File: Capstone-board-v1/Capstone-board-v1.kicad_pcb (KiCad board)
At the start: 2 copper layers, 22 parts, among them J1 Pico Socket 1, J2 Pico Socket 2, M1 DC Vibration Motor, Q1 2N3904, U1 3.3 V Voltage Regulator, U2 555 Timer, U3 Gyroscope Sensor, U4 OP-Amp, U5 Hall Effect Sensor

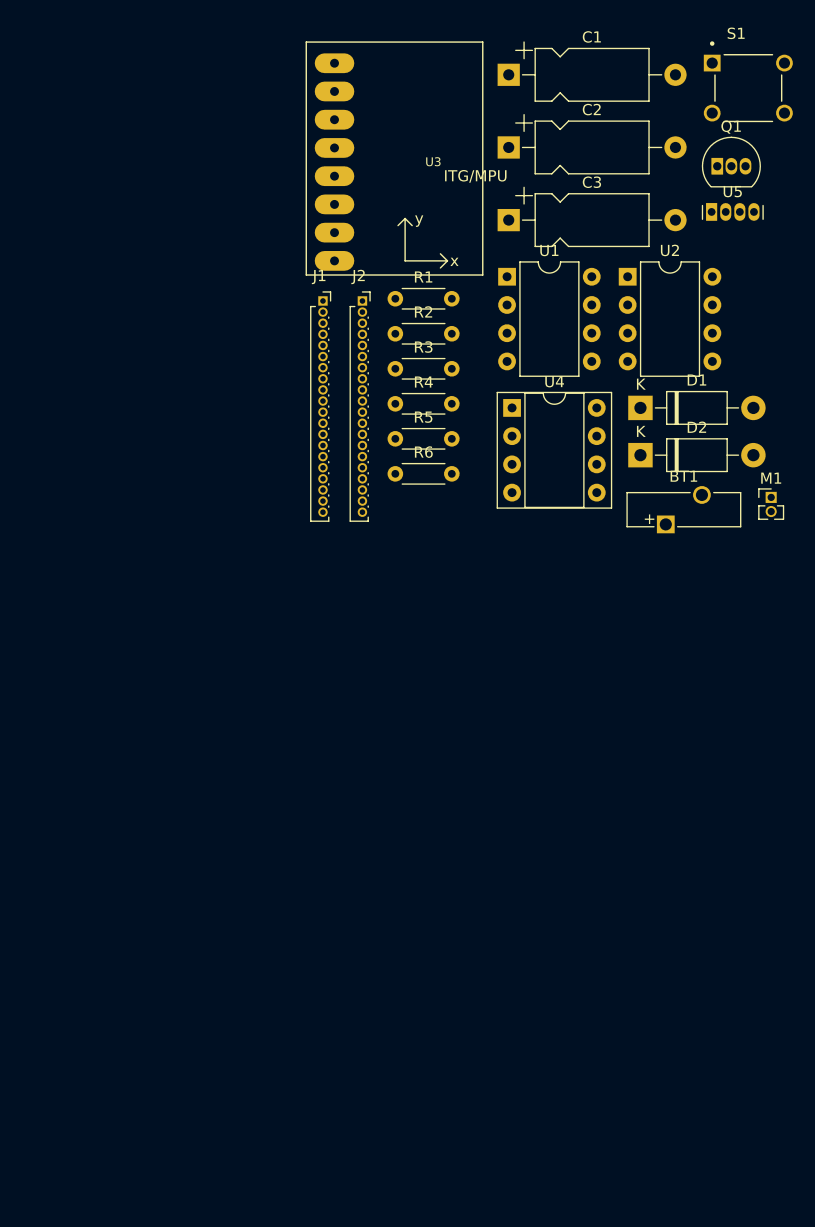
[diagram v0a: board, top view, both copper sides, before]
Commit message: correct hole size
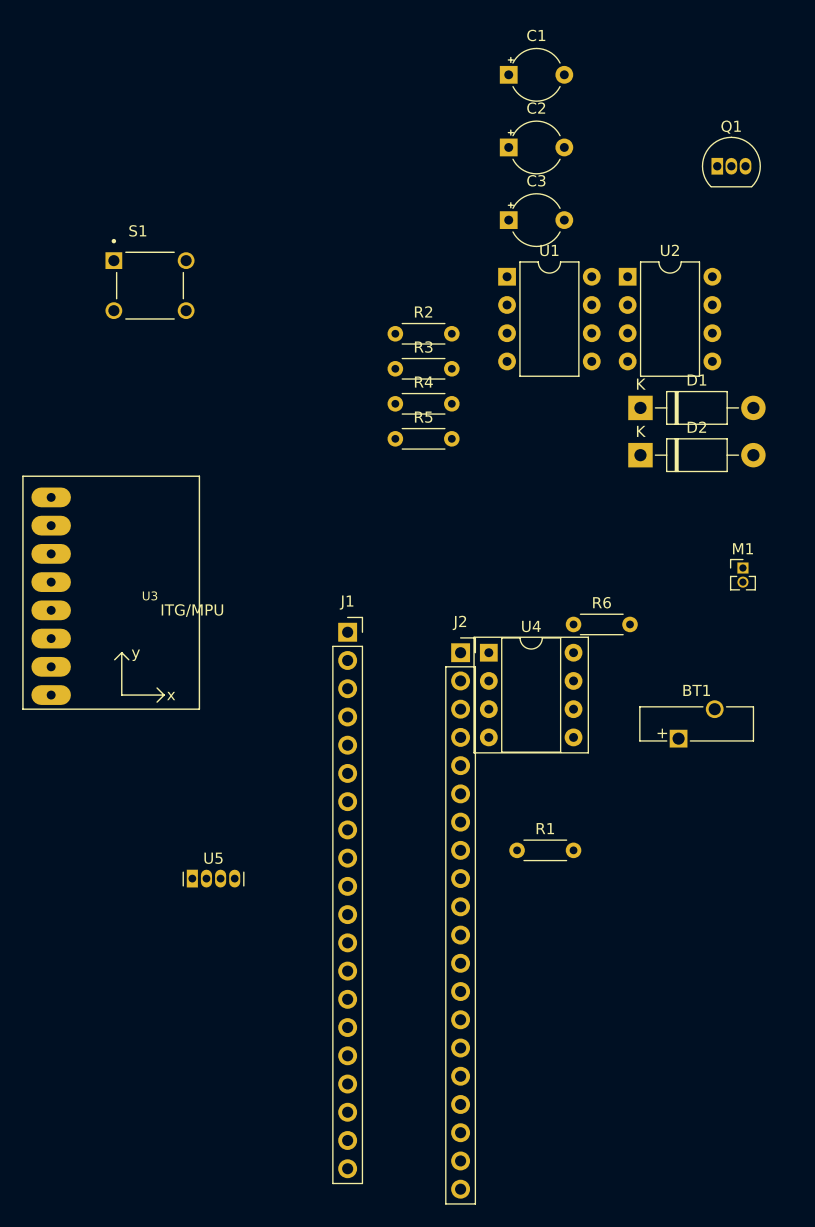
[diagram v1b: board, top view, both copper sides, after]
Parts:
- C1, C2, C3: footprint Capacitor_THT:CP_Axial_L10.0mm_D4.5mm_P15.00mm_Horizontal -> Capacitor_THT:CP_Radial_Tantal_D4.5mm_P5.00mm
- J1, J2: footprint Connector_PinSocket_1.00mm:PinSocket_1x20_P1.00mm_Vertical -> Connector_PinSocket_2.54mm:PinSocket_1x20_P2.54mm_Vertical
- moved U5 76.0 mm to (113.0, 121.9)
- moved S1 56.7 mm to (109.2, 68.6)
- moved R1 50.8 mm to (142.2, 119.4)
- moved U3 46.6 mm to (109.2, 96.5)
- moved J2 32.8 mm to (137.2, 101.6)
- moved J1 29.9 mm to (127.0, 99.8)
- moved U4 22.1 mm to (139.7, 101.6)
- moved R6 21.0 mm to (147.3, 99.1)
- moved BT1 19.3 mm to (156.8, 109.3)
- moved M1 6.84 mm to (162.6, 94.0)

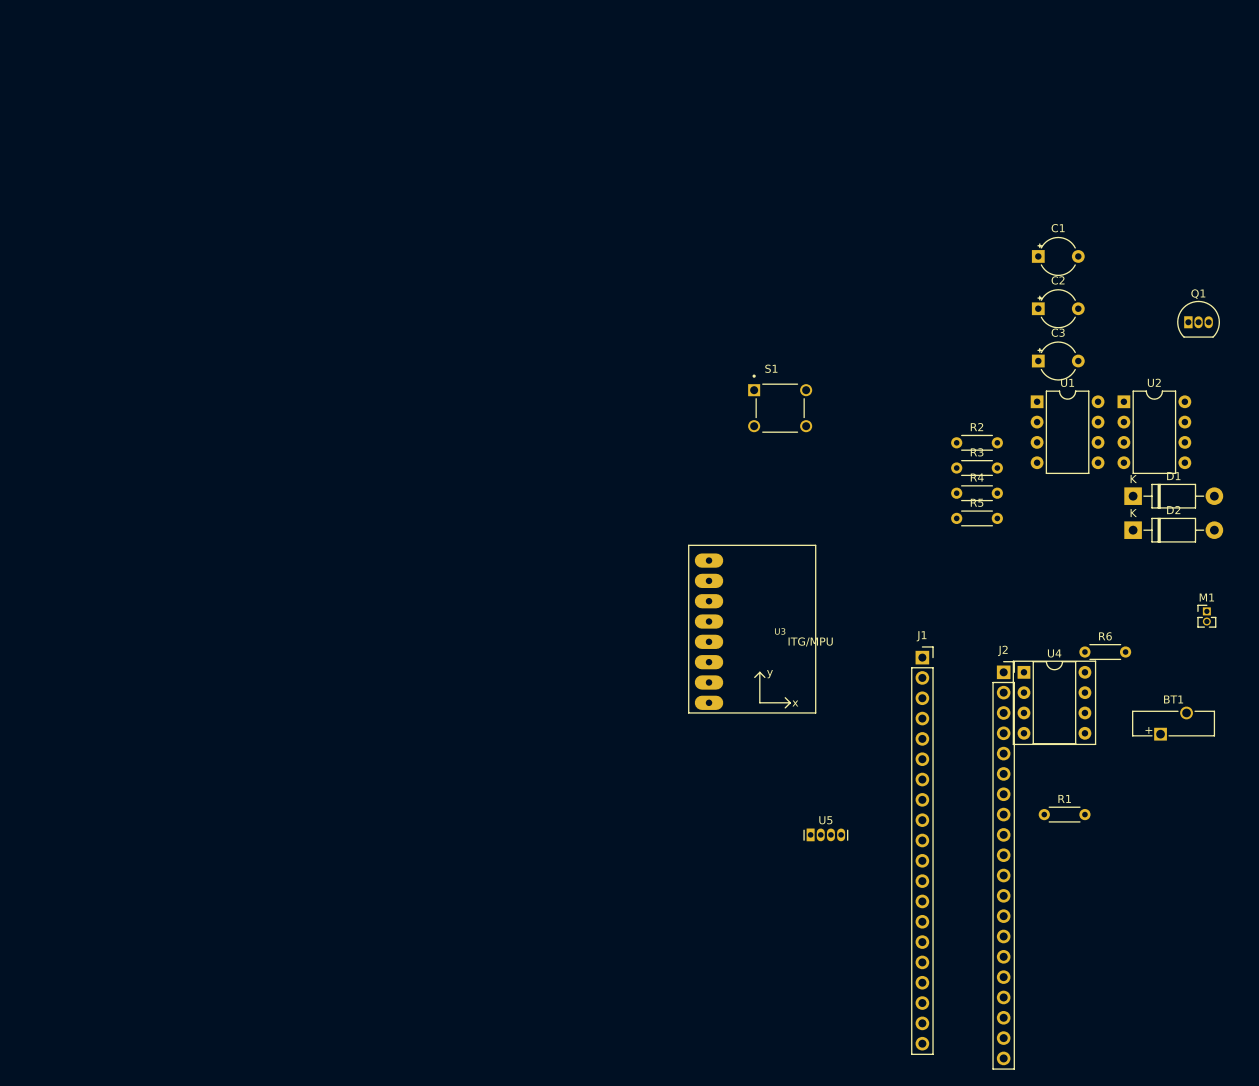
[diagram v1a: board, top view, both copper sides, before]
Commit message: traces added
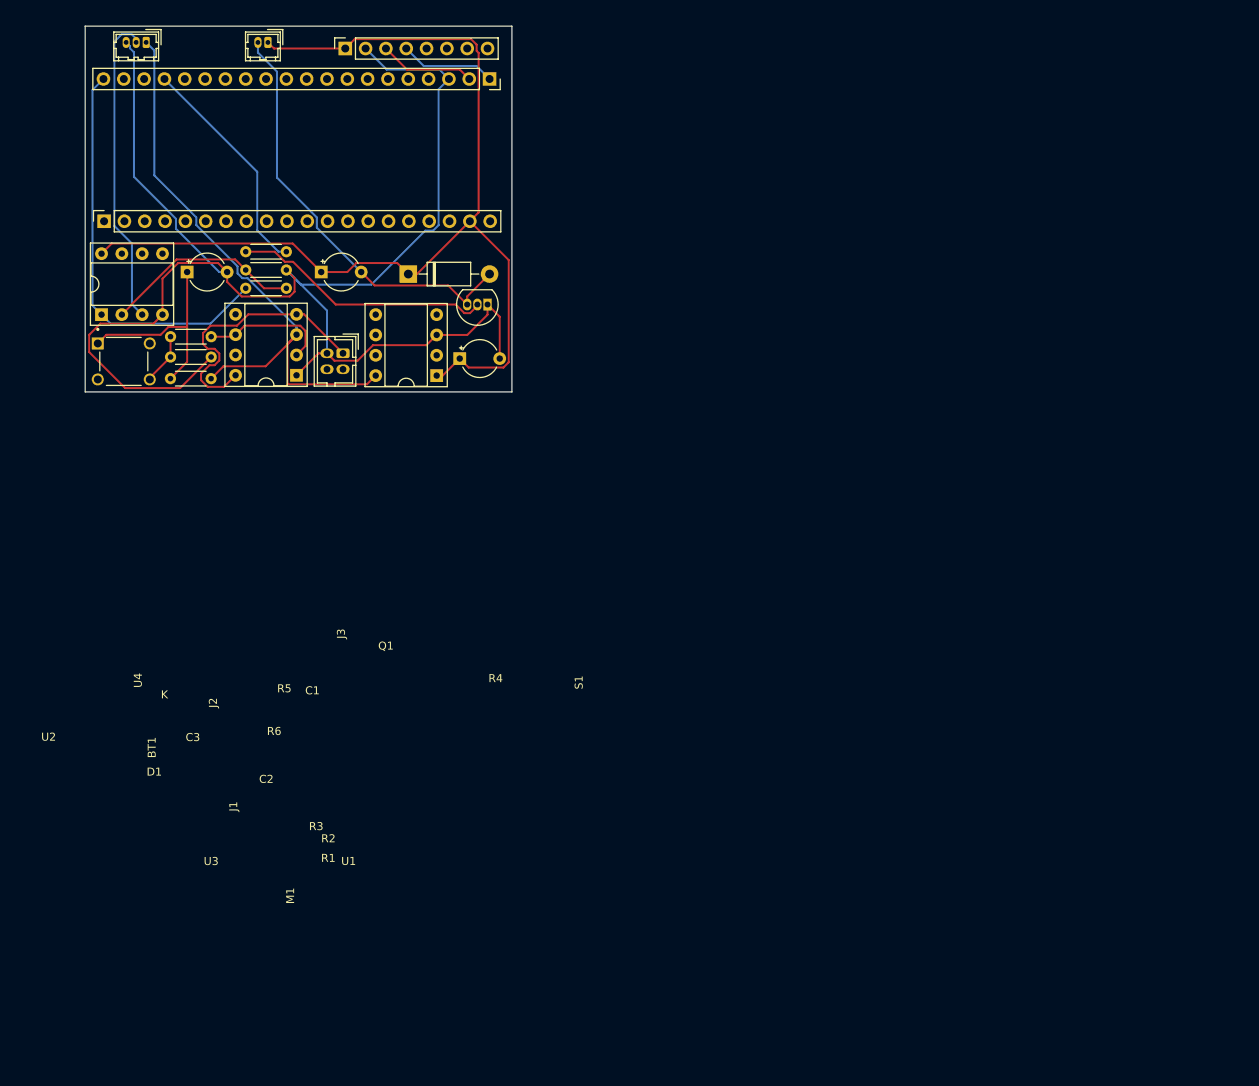
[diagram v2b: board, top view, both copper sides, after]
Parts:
- removed the D1 at (153.3, 79.6)
- removed the U3 at (109.2, 96.5)
- added J3: Gyroscope Sensor, Connector_PinSocket_2.54mm:PinSocket_1x08_P2.54mm_Vertical, F.Cu at (54.9, 23.6)
- BT1: footprint Battery:Battery_Panasonic_CR1025-VSK_Vertical_CircularHoles -> Connector_Hirose:Hirose_DF11-4DP-2DSA_2x02_P2.00mm_Vertical
- M1: footprint Connector_PinHeader_1.27mm:PinHeader_1x02_P1.27mm_Vertical -> Connector_Hirose:Hirose_DF13-02P-1.25DSA_1x02_P1.25mm_Vertical
- S1: footprint TS02-66-60-BK-100-LCR-D:SW_TS02-66-60-BK-160-LCR-D -> TS:SW_TS02-66-60-BK-160-LCR-D
- U1, U2: footprint Package_DIP:DIP-8_W7.62mm -> Package_DIP:DIP-8_W7.62mm_Socket
- U3: renamed from U5; footprint Sensor_Current:Allegro_SIP-4 -> Connector_Hirose:Hirose_DF13-03P-1.25DSA_1x03_P1.25mm_Vertical
- U4: value OP-Amp -> OP Amp
- moved M1 137.2 mm to (45.2, 22.9), turned to 180 degrees
- moved U3 129.3 mm to (30.0, 22.9), turned to 180 degrees
- moved J2 125.8 mm to (24.7, 45.2), turned to 90 degrees
- moved U4 123.7 mm to (24.4, 56.9), turned to 90 degrees
- moved R1 122.1 mm to (33.0, 64.9)
- moved R6 114.3 mm to (42.4, 53.6)
- moved BT1 112.7 mm to (54.6, 61.7), turned to -90 degrees
- moved C1 106.4 mm to (35.1, 51.6)
- moved U2 103.5 mm to (48.8, 64.5), turned to 180 degrees
- moved R3 99.6 mm to (33.0, 59.6)
- moved D1 96.1 mm to (62.7, 51.8)
- moved R5 94.1 mm to (42.4, 51.3)
- moved R4 93.9 mm to (42.4, 49.0)
- moved R2 93.8 mm to (38.1, 62.2), turned to 180 degrees
- moved J1 90.3 mm to (72.9, 27.4), turned to -90 degrees
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- renumbered D2 to D1
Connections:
- C2 pad 1: Net-(D2-K) -> Net-(D1-K)
- C3 pad 1: Net-(D2-K) -> Net-(D1-K)
- D1 pad 1: Net-(D2-K) -> Net-(D1-K)
- J2 pad 19: Net-(D2-K) -> Net-(D1-K)
- M1 pad 1: Net-(D2-K) -> Net-(D1-K)
- R1 pad 2: Net-(D1-A) (its old number) -> Net-(U1-IN)
- U1 pad 1: Net-(D2-K) -> Net-(D1-K)
- U1 pad 8: Net-(D1-K) -> Net-(U1-IN)
- U2 pad 3: Net-(D1-A) (its old number) -> Net-(U1-IN)
- U3 pad 1: VCC -> Net-(U1-IN)
- U3 pad 3: unconnected-(U5-NC-Pad3) -> Earth
- U4 pad 4: (no net) -> Earth
- U4 pad 8: (no net) -> Net-(D1-K)
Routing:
- net Earth: track 0.00 -> 195.9 mm
- net Net-(D1-K): track 0.00 -> 131.9 mm
- net Net-(U1-IN): track 0.00 -> 75.9 mm
- net Net-(D1-A): track 0.00 -> 53.9 mm
- net Net-(J1-Pin_20): track 0.00 -> 50.8 mm
- net Net-(U3-VOUT): track 0.00 -> 39.8 mm
- net VCC: track 0.00 -> 34.3 mm
- net Net-(Q1-B): track 0.00 -> 32.7 mm
- net Net-(J1-Pin_17): track 0.00 -> 28.5 mm
- net Net-(C1-Pad1): track 0.00 -> 26.4 mm
- net Net-(U4--): track 0.00 -> 24.9 mm
- net Net-(U2-THR): track 0.00 -> 16.1 mm
- net Net-(J1-Pin_2): track 0.00 -> 12.0 mm
- net Net-(J1-Pin_1): track 0.00 -> 12.0 mm
- net Net-(R2-Pad2): track 0.00 -> 6.42 mm
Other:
- board outline added: 53.3 x 45.7 mm

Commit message: All routing done.
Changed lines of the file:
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@@
         (effects (font (size 1 1) (thickness 0.15)))
     )
-    (fp_text value "Hall Effect Sensor" (at 7.62 -68.326) (layer "F.Fab")
+    (fp_text value "Hall Effect Sensor" (at 7.62 -68.326) (layer "F.SilkS")
         (effects (font (size 1 1) (thickness 0.15)))
     )
@@
         (effects (font (size 1 1) (thickness 0.15)))
     )
-    (fp_text value "OP Amp" (at -44.206 16.754 90) (layer "F.Fab")
-        (effects (font (size 1 1) (thickness 0.15)))
-    )
+    (fp_text value "OP Amp" (at -32.522 18.532 90) (layer "F.Fab")
+        (effects (font (size 1 1) (thickness 0.15)))
+    )

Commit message: Final traces done
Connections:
- R2 pad 2: Net-(R2-Pad2) -> Net-(U2-THR)
- R3 pad 1: Net-(R2-Pad2) -> Net-(U2-THR)
- R3 pad 2: Net-(U2-THR) -> VCC
- S1 pad 4: Net-(R2-Pad2) -> Net-(U2-THR)
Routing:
- net Net-(U2-THR): track 16.1 -> 28.8 mm
- net Net-(R2-Pad2): track 6.42 -> 0.00 mm
- net VCC: track 34.3 -> 28.5 mm

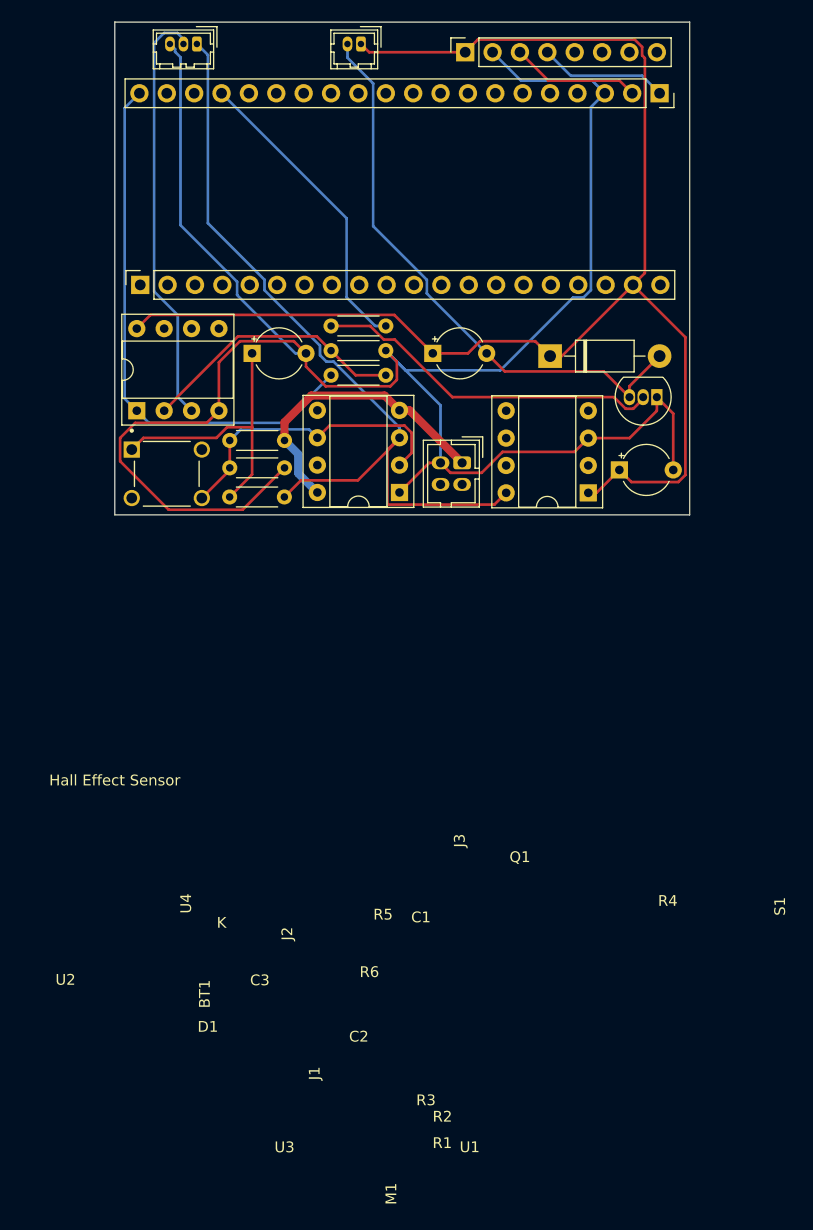
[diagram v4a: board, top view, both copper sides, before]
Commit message: reference designators added
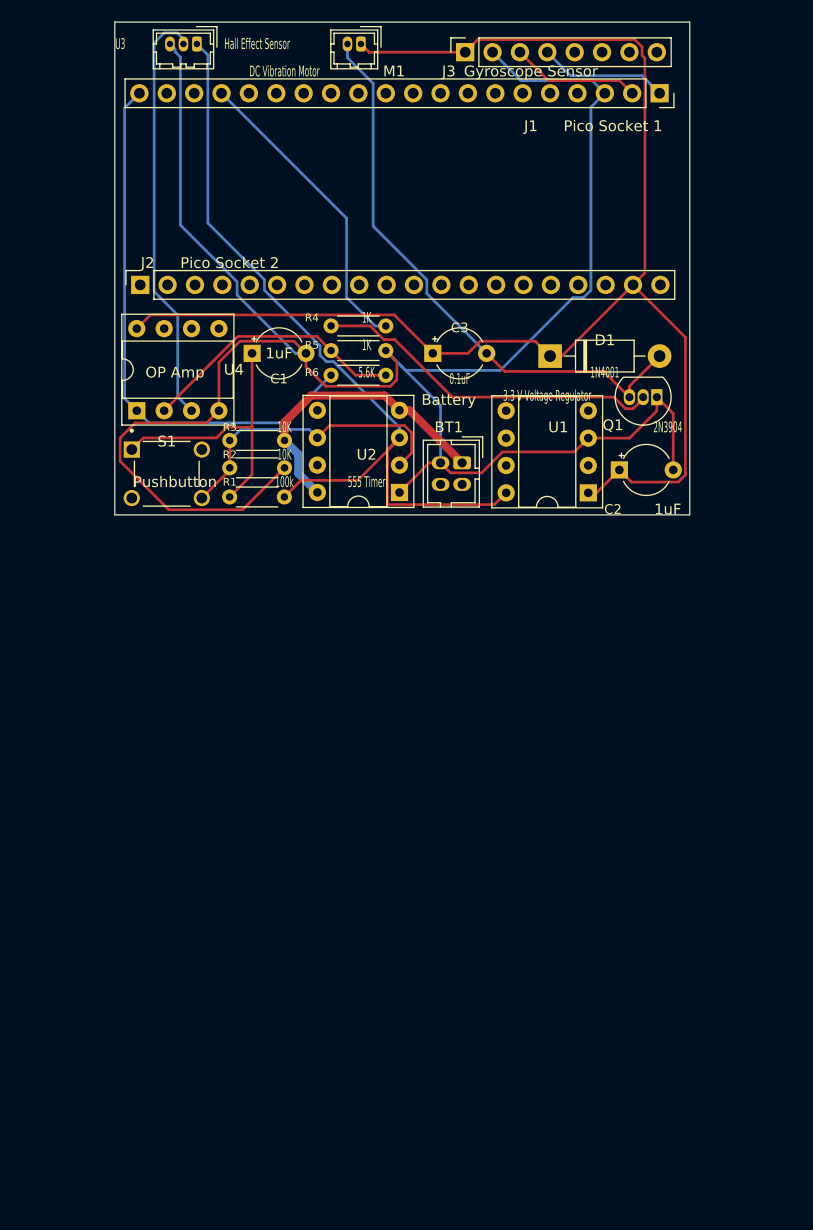
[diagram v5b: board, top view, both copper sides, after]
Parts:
- R1: value 100kOhms -> 100k
- R2, R3: value 10KOhms -> 10K
- R4, R5: value 1KOhms -> 1K
- R6: value 5.6KOhms -> 5.6K

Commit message: Final PCB completed!
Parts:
- U1: value 3.3 V Voltage Regulator -> 3.3 V V.R
- moved R1 0.42 mm to (33.0, 65.3)
- moved R2 0.30 mm to (38.1, 62.5)
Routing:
- net Net-(U1-IN): track 75.9 -> 99.4 mm
- net VCC: track 28.5 -> 31.2 mm
- net Net-(D1-K): track 131.9 -> 133.9 mm
- net Earth: track 195.9 -> 193.9 mm
- net Net-(U3-VOUT): track 39.8 -> 40.8 mm
- net Net-(U2-THR): track 28.8 -> 29.7 mm
- net Net-(Q1-B): track 32.7 -> 33.5 mm
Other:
- board size 53.3 x 45.7 mm -> 53.6 x 46.5 mm

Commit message: Final PCB's done.
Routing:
- net Net-(D1-K): track 133.9 -> 137.8 mm
- net Net-(U1-IN): track 99.4 -> 98.5 mm
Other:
- board size 53.6 x 46.5 mm -> 53.9 x 47.3 mm
- board text added: "Capstone Fall 2023: Epitome | Team Members: Ruhul Quddus, Goutham Mittadhoddi, Nima Razavi, Ian Le, Kenny Zhang"
